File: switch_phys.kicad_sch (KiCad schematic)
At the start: 36 parts, among them J1 0826-1X4T-43-F

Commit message: minor footprint fixing
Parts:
- J1: manf# L826-1X4T-43-F -> (none)
- U1: footprint Package_QFP:TQFP-128_14x14mm_P0.4mm -> KL:TQFP-128_14x14mm_P0.4mm_with_EPAD; symbol lan9645xF:lan9645xF_128_TQFP -> KL_IC_LAN9645xF:lan9645xF_128_TQFP; Digikey (none) -> 150-LAN96455FT-I/8MWTR-ND; Mouser (none) -> 579-LAN96455FTI8MW; manf# LAN96455F-I/8MW -> (none)
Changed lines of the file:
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@@
 		)
 	)
-	(text_box "The assumption is that the VDD_IO will be 3.3V not 1.8V, not 2.5V"
+	(text_box "The assumption, for the LEDS is that the VDD_IO will be 3.3V not 1.8V, not 2.5V"
 		(exclude_from_sim no)
 		(at 252.73 168.91 0)
@@
 			)
 		)
-		(property "manf#" "L826-1X4T-43-F"
-			(at 148.59 165.1 90)
-			(effects
-				(font
-					(size 1.27 1.27)
-				)
-				(hide yes)
-			)
-		)
 		(pin "1_1"
 		)
@@
 		(fields_autoplaced yes)
 		(property "Reference" "R7"
-			(at 167.6087 37.9633 0)
+			(at 167.64 37.9633 0)
 			(effects
 				(font
@@
 		)
 		(property "Value" "1K"
-			(at 167.6087 40.5033 0)
+			(at 167.64 40.5033 0)
 			(effects
 				(font
@@
 			)
 		)
-		(property "manf#" "L826-1X4T-43-F"
-			(at 106.68 25.4 90)
-			(effects
-				(font
-					(size 1.27 1.27)
-				)
-				(hide yes)
-			)
-		)
 		(pin "1_1"
 		)
@@
 			)
 		)
-		(property "manf#" "L826-1X4T-43-F"
-			(at 162.56 62.23 90)
-			(effects
-				(font
-					(size 1.27 1.27)
-				)
-				(hide yes)
-			)
-		)
 		(pin "1_1"
 		)
@@
 	)
 	(symbol
-		(lib_id "lan9645xF:lan9645xF_128_TQFP")
+		(lib_id "KL_IC_LAN9645xF:lan9645xF_128_TQFP")
 		(at 67.31 157.48 180)
 		(unit 3)
@@
 			)
 		)
-		(property "Footprint" "Package_QFP:TQFP-128_14x14mm_P0.4mm"
-			(at 67.31 157.48 0)
+		(property "Footprint" "KL:TQFP-128_14x14mm_P0.4mm_with_EPAD"
+			(at 53.594 163.322 0)
 			(effects
 				(font
@@
 			)
 		)
-		(property "manf#" "LAN96455F-I/8MW"
+		(property "Mouser" "579-LAN96455FTI8MW "
+			(at 54.356 165.608 0)
+			(effects
+				(font
+					(size 1.27 1.27)
+				)
+				(hide yes)
+			)
+		)
+		(property "Digikey" "150-LAN96455FT-I/8MWTR-ND"
+			(at 67.31 157.48 0)
+			(effects
+				(font
+					(size 1.27 1.27)
+				)
+				(hide yes)
+			)
+		)
+		(property "LSCS" ""
 			(at 67.31 157.48 0)
 			(effects
@@
 				(hide yes)
 			)
-		)
-		(property "manf#" "L826-1X4T-43-F"
-			(at 195.58 128.27 90)
-			(effects
-				(font
-					(size 1.27 1.27)
-				)
-				(hide yes)
-			)

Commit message: This commit intends to fix multiple issues:
 - 1.1 -> 1.15 v buck rails
 - Revision consistently using Rev. A
 - Issue with the Switch symbol when moving library
 - Adding new footprint and symbol for 2.54mm Headers
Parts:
- U1: footprint KL:TQFP-128_14x14mm_P0.4mm_with_EPAD -> Package_QFP:TQFP-128_14x14mm_P0.4mm; Digikey 150-LAN96455FT-I/8MWTR-ND -> (none); Mouser 579-LAN96455FTI8MW -> (none); manf# (none) -> LAN96455F-I/8MW

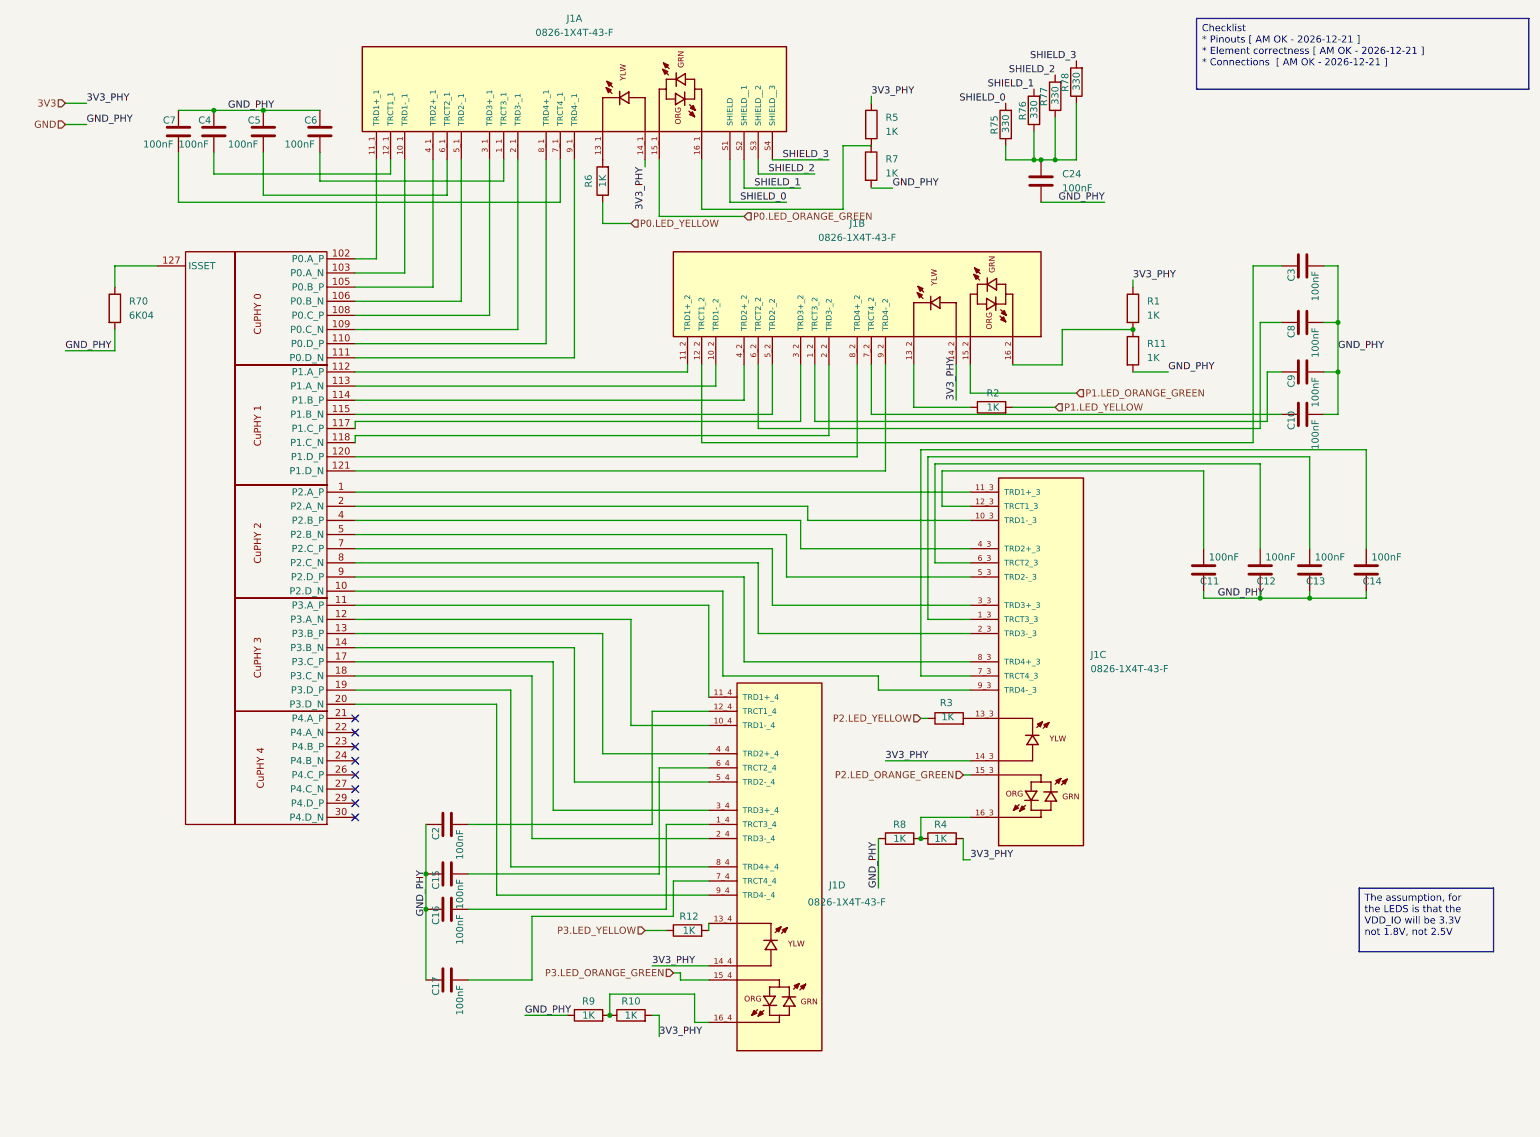
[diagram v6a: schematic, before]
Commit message: fixing issue related to symbol changes, and updating components
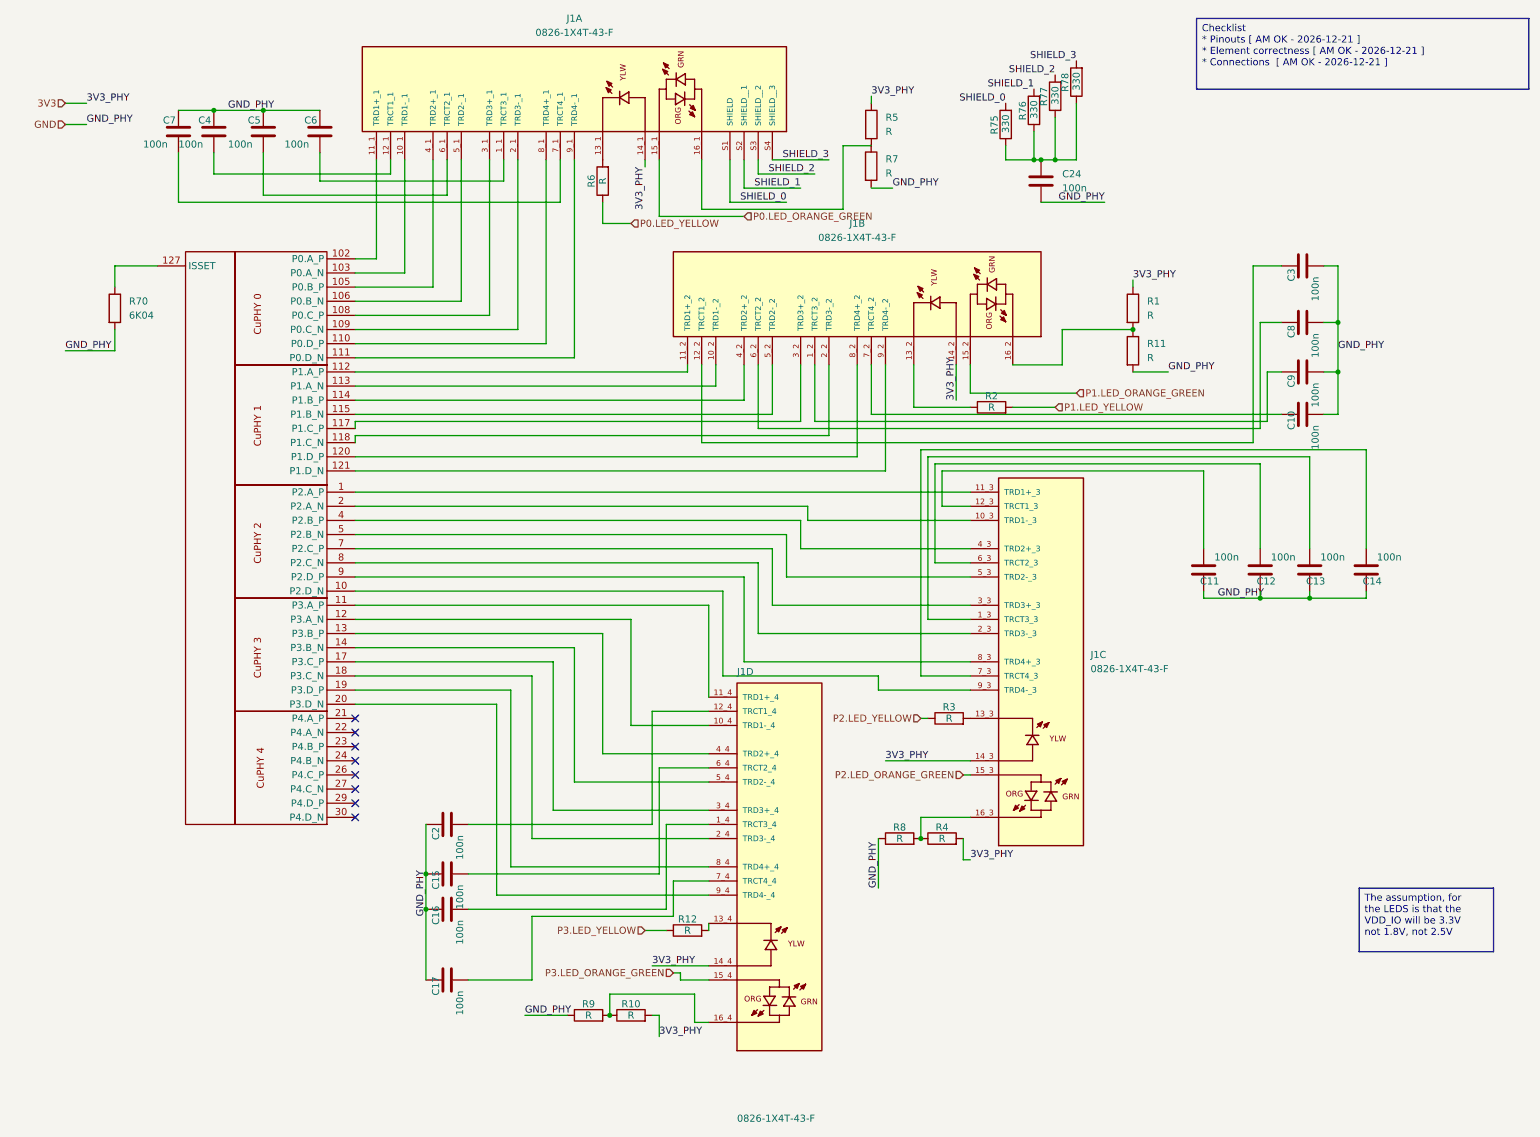
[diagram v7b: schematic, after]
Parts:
- C10, C11, C12, C13, C14, C15, C16, C17, C2, C24, C3, C4, C5, C6, C7, C8, C9: value 100nF -> 100n; footprint KL:C_0603 -> Capacitor_SMD:C_0201_0603Metric; symbol KL_C:C_100nF_50V_X7R_0603_10 -> KL_C:C_100n_50V_X7R_0603_10; Tolerance 10 -> 20; Voltage 50 -> 10
- J1: symbol ethernet-magjack:0826-1X4T-43-F -> KL_Connectors_RJ45:0826-1X4T-43-F
- R1, R10, R11, R12, R2, R3, R4, R5, R6, R7, R8, R9: value 1K -> R; footprint KL:R_0603 -> KL_Footprints:C_0603; symbol KL_R:R_1K_125mW_5_0603 -> KL_R:R_1K_100mW_5_0603; Digikey 2019-RK73B1JTTDB102JCT-ND -> A130091CT-ND; LCSC C131707 -> C4112612; Mouser 660-RK73B1JTTDB102J -> 279-CRGCQ0603J1K0; Power 125mW -> 100mW
- R70, R75, R76, R77, R78: footprint KL:R_0603 -> KL_Footprints:C_0603

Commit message: cleans up PHY section and moves connectors into separate subpages
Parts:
- removed C10, C11, C12, C13, C14, C15, C16, C17, C2, C24, C3, C4, C5, C6, C7, C8, C9: 100n, Capacitor_SMD:C_0201_0603Metric, symbol KL_C:C_100n_50V_X7R_0603_10
- removed J1: 0826-1X4T-43-F, 0826-1X4T-43-F:BEL_0826-1X4T-43-F, symbol KL_Connectors_RJ45:0826-1X4T-43-F
- removed R1, R10, R11, R12, R2, R3, R4, R5, R6, R7, R8, R9: R, KL_Footprints:C_0603, symbol KL_R:R_1K_100mW_5_0603
- removed R75, R76, R77, R78: 330, KL_Footprints:C_0603, symbol KL_R:R_330R_100mW_1_0603
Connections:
- net RJ45_Connector_Port3/TRD1-_3: now reaches U1.12 (P3.A_N)
- net RJ45_Connector_Port3/TRD1+_3: now reaches U1.11 (P3.A_P)
- net RJ45_Connector_Port3/TRD3-_3: now reaches U1.18 (P3.C_N)
- net RJ45_Connector_Port3/TRD3+_3: now reaches U1.17 (P3.C_P)
- net RJ45_Connector_Port3/TRD2+_3: now reaches U1.13 (P3.B_P)
- net RJ45_Connector_Port3/TRD2-_3: now reaches U1.14 (P3.B_N)
- net RJ45_Connector_Port3/TRD4+_3: now reaches U1.19 (P3.D_P)
- net RJ45_Connector_Port3/TRD4-_3: now reaches U1.20 (P3.D_N)
- net RJ45_Connector_Port2/TRD1+_2: now reaches U1.1 (P2.A_P)
- net RJ45_Connector_Port2/TRD4-_2: now reaches U1.10 (P2.D_N)
- net RJ45_Connector_Port0/TRD1+_0: now reaches U1.102 (P0.A_P)
- net RJ45_Connector_Port0/TRD1-_0: now reaches U1.103 (P0.A_N)
- net RJ45_Connector_Port0/TRD2+_0: now reaches U1.105 (P0.B_P)
- net RJ45_Connector_Port0/TRD2-_0: now reaches U1.106 (P0.B_N)
- net RJ45_Connector_Port0/TRD3+_0: now reaches U1.108 (P0.C_P)
- net RJ45_Connector_Port0/TRD3-_0: now reaches U1.109 (P0.C_N)
- net RJ45_Connector_Port0/TRD4+_0: now reaches U1.110 (P0.D_P)
- net RJ45_Connector_Port0/TRD4-_0: now reaches U1.111 (P0.D_N)
- net RJ45_Connector_Port1/TRD1+_1: now reaches U1.112 (P1.A_P)
- net RJ45_Connector_Port1/TRD1-_1: now reaches U1.113 (P1.A_N)
- net RJ45_Connector_Port1/TRD2+_1: now reaches U1.114 (P1.B_P)
- net RJ45_Connector_Port1/TRD2-_1: now reaches U1.115 (P1.B_N)
- net RJ45_Connector_Port1/TRD3+_1: now reaches U1.117 (P1.C_P)
- net RJ45_Connector_Port1/TRD3-_1: now reaches U1.118 (P1.C_N)
- net RJ45_Connector_Port1/TRD4+_1: now reaches U1.120 (P1.D_P)
- net RJ45_Connector_Port1/TRD4-_1: now reaches U1.121 (P1.D_N)
- net RJ45_Connector_Port2/TRD1-_2: now reaches U1.2 (P2.A_N)
- net RJ45_Connector_Port2/TRD2+_2: now reaches U1.4 (P2.B_P)
- net RJ45_Connector_Port2/TRD2-_2: now reaches U1.5 (P2.B_N)
- net RJ45_Connector_Port2/TRD3+_2: now reaches U1.7 (P2.C_P)
- net RJ45_Connector_Port2/TRD3-_2: now reaches U1.8 (P2.C_N)
- net RJ45_Connector_Port2/TRD4+_2: now reaches U1.9 (P2.D_P)
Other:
- added sheet RJ45_Connector_Port0 (RJ45_Connector_Port0.kicad_sch)
- added sheet RJ45_Connector_Port1 (RJ45_Connector_Port1.kicad_sch)
- added sheet RJ45_Connector_Port2 (RJ45_Connector_Port2.kicad_sch)
- added sheet RJ45_Connector_Port3 (RJ45_Connector_Port3.kicad_sch)
- moved on the sheet: R70
